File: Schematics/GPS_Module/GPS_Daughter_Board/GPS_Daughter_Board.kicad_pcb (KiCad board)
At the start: 2 copper layers, 50 x 65 mm, 22 parts, among them J2 470804001, U1 SAM-M10Q, U2 LM66100DCKR

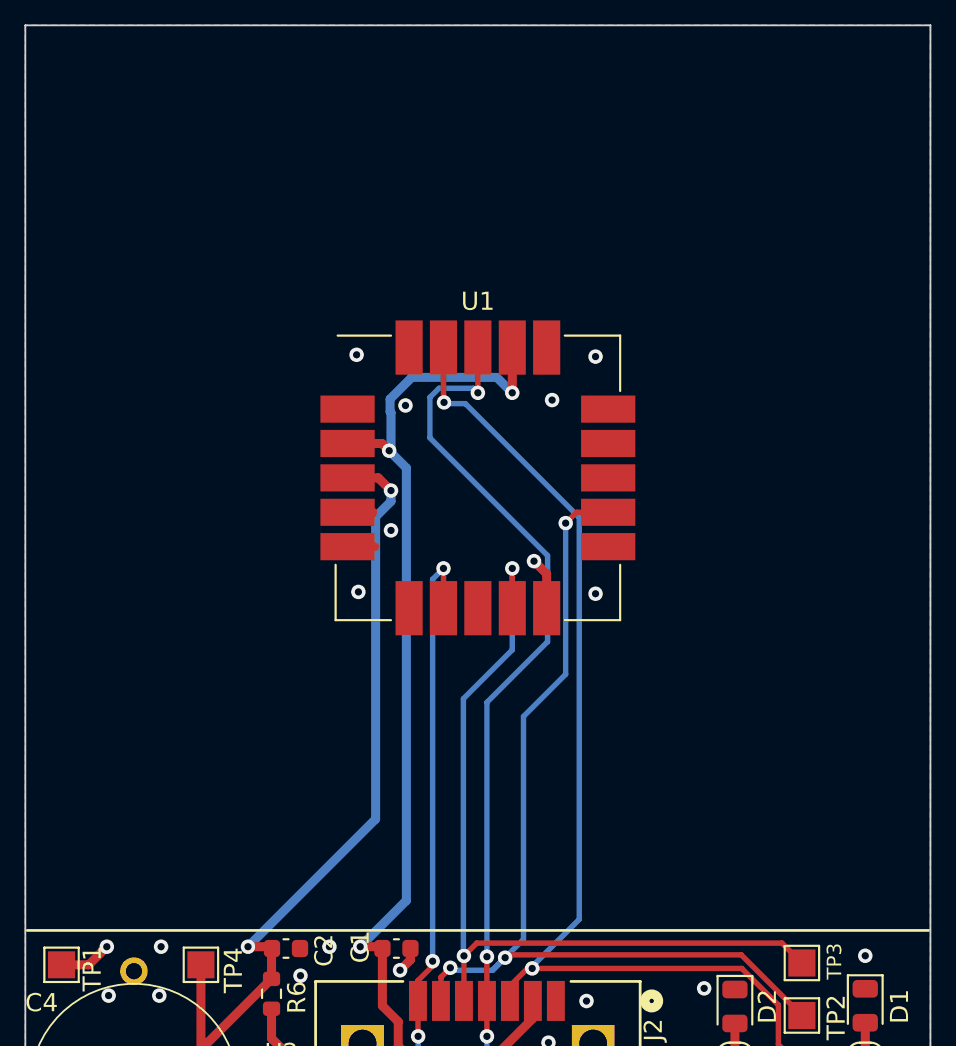
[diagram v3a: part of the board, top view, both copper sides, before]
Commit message: acutally finished GND stitching
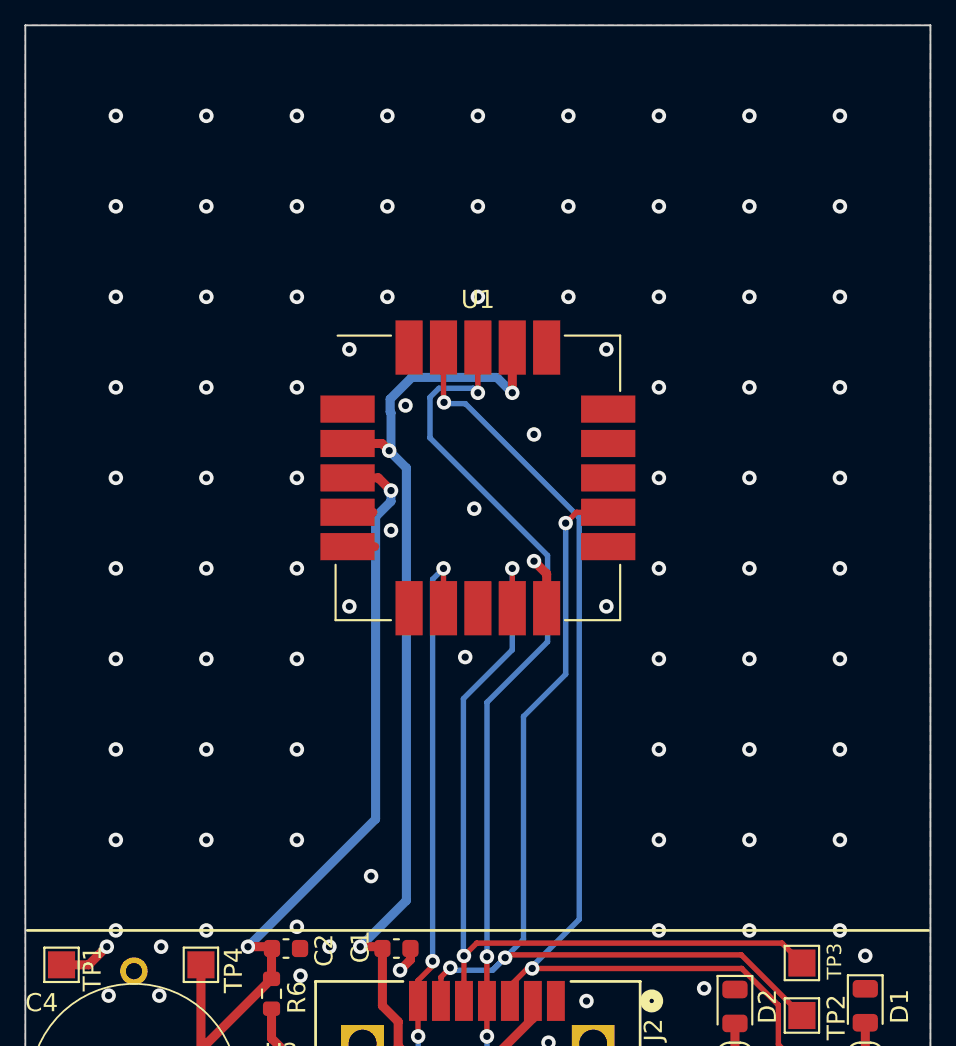
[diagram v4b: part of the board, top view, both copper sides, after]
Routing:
- net GPS_GND: vias 20 -> 92
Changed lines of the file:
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@@
     (property "ki_keywords" "gps module with antenna")
     (attr smd)
-    (fp_text reference "U1" (at 0 -9.75) (layer "F.SilkS")
+    (fp_text reference "U1" (at 0 -9.85) (layer "F.SilkS")
         (effects (font (size 1 1) (thickness 0.15)))
     )
@@
   (segment (start 142.0005 103) (end 140.5 103) (width 0.5) (layer "F.Cu") (net 1))
   (segment (start 141.9005 101.1) (end 140.5 101.1) (width 0.5) (layer "F.Cu") (net 1))
-  (via (at 154.2 105.6) (size 0.8) (drill 0.4) (layers "F.Cu" "B.Cu") (free) (net 1))
-  (via (at 141.1 105.5) (size 0.8) (drill 0.4) (layers "F.Cu" "B.Cu") (free) (net 1))
+  (via (at 132.7 104.2) (size 0.8) (drill 0.4) (layers "F.Cu" "B.Cu") (free) (net 1))
+  (via (at 152.7 79.2) (size 0.8) (drill 0.4) (layers "F.Cu" "B.Cu") (free) (net 1))
+  (via (at 127.7 99.2) (size 0.8) (drill 0.4) (layers "F.Cu" "B.Cu") (free) (net 1))
+  (via (at 137.7 104.2) (size 0.8) (drill 0.4) (layers "F.Cu" "B.Cu") (free) (net 1))
+  (via (at 154.8 106.3) (size 0.8) (drill 0.4) (layers "F.Cu" "B.Cu") (free) (net 1))
+  (via (at 127.7 124.2) (size 0.8) (drill 0.4) (layers "F.Cu" "B.Cu") (free) (net 1))
+  (via (at 137.7 114.2) (size 0.8) (drill 0.4) (layers "F.Cu" "B.Cu") (free) (net 1))
+  (via (at 140.6 106.3) (size 0.8) (drill 0.4) (layers "F.Cu" "B.Cu") (free) (net 1))
+  (via (at 127.7 94.2) (size 0.8) (drill 0.4) (layers "F.Cu" "B.Cu") (free) (net 1))
   (via (at 130.2 125.1) (size 0.8) (drill 0.4) (layers "F.Cu" "B.Cu") (free) (net 1))
+  (via (at 127.7 109.2) (size 0.8) (drill 0.4) (layers "F.Cu" "B.Cu") (free) (net 1))
+  (via (at 157.7 79.2) (size 0.8) (drill 0.4) (layers "F.Cu" "B.Cu") (free) (net 1))
+  (via (at 167.7 89.2) (size 0.8) (drill 0.4) (layers "F.Cu" "B.Cu") (free) (net 1))
+  (via (at 137.7 119.2) (size 0.8) (drill 0.4) (layers "F.Cu" "B.Cu") (free) (net 1))
+  (via (at 162.7 94.2) (size 0.8) (drill 0.4) (layers "F.Cu" "B.Cu") (free) (net 1))
+  (via (at 157.7 114.2) (size 0.8) (drill 0.4) (layers "F.Cu" "B.Cu") (free) (net 1))
+  (via (at 152.7 89.2) (size 0.8) (drill 0.4) (layers "F.Cu" "B.Cu") (free) (net 1))
+  (via (at 147.7 89.2) (size 0.8) (drill 0.4) (layers "F.Cu" "B.Cu") (free) (net 1))
+  (via (at 142.7 84.2) (size 0.8) (drill 0.4) (layers "F.Cu" "B.Cu") (free) (net 1))
+  (via (at 162.7 79.2) (size 0.8) (drill 0.4) (layers "F.Cu" "B.Cu") (free) (net 1))
+  (via (at 167.7 109.2) (size 0.8) (drill 0.4) (layers "F.Cu" "B.Cu") (free) (net 1))
+  (via (at 167.7 79.2) (size 0.8) (drill 0.4) (layers "F.Cu" "B.Cu") (free) (net 1))
+  (via (at 147.7 79.2) (size 0.8) (drill 0.4) (layers "F.Cu" "B.Cu") (free) (net 1))
+  (via (at 162.7 84.2) (size 0.8) (drill 0.4) (layers "F.Cu" "B.Cu") (free) (net 1))
+  (via (at 137.7 89.2) (size 0.8) (drill 0.4) (layers "F.Cu" "B.Cu") (free) (net 1))
+  (via (at 157.7 109.2) (size 0.8) (drill 0.4) (layers "F.Cu" "B.Cu") (free) (net 1))
   (via (at 143.7 95.2) (size 0.8) (drill 0.4) (layers "F.Cu" "B.Cu") (free) (net 1))
+  (via (at 132.7 109.2) (size 0.8) (drill 0.4) (layers "F.Cu" "B.Cu") (free) (net 1))
+  (via (at 137.7 94.2) (size 0.8) (drill 0.4) (layers "F.Cu" "B.Cu") (free) (net 1))
+  (via (at 127.7 84.2) (size 0.8) (drill 0.4) (layers "F.Cu" "B.Cu") (free) (net 1))
+  (via (at 167.7 124.2) (size 0.8) (drill 0.4) (layers "F.Cu" "B.Cu") (free) (net 1))
   (via (at 127.2 125.1) (size 0.8) (drill 0.4) (layers "F.Cu" "B.Cu") (free) (net 1))
+  (via (at 142.7 79.2) (size 0.8) (drill 0.4) (layers "F.Cu" "B.Cu") (free) (net 1))
+  (via (at 137.7 99.2) (size 0.8) (drill 0.4) (layers "F.Cu" "B.Cu") (free) (net 1))
+  (via (at 127.7 114.2) (size 0.8) (drill 0.4) (layers "F.Cu" "B.Cu") (free) (net 1))
   (via (at 153.7 128.1) (size 0.8) (drill 0.4) (layers "F.Cu" "B.Cu") (free) (net 1))
+  (via (at 132.7 114.2) (size 0.8) (drill 0.4) (layers "F.Cu" "B.Cu") (free) (net 1))
+  (via (at 132.7 124.2) (size 0.8) (drill 0.4) (layers "F.Cu" "B.Cu") (free) (net 1))
+  (via (at 157.7 119.2) (size 0.8) (drill 0.4) (layers "F.Cu" "B.Cu") (free) (net 1))
   (via (at 151.6 130.4) (size 0.8) (drill 0.4) (layers "F.Cu" "B.Cu") (free) (net 1))
+  (via (at 152.7 84.2) (size 0.8) (drill 0.4) (layers "F.Cu" "B.Cu") (free) (net 1))
+  (via (at 132.7 119.2) (size 0.8) (drill 0.4) (layers "F.Cu" "B.Cu") (free) (net 1))
   (via (at 130.1 127.8) (size 0.8) (drill 0.4) (layers "F.Cu" "B.Cu") (free) (net 1))
+  (via (at 157.7 104.2) (size 0.8) (drill 0.4) (layers "F.Cu" "B.Cu") (free) (net 1))
+  (via (at 132.7 99.2) (size 0.8) (drill 0.4) (layers "F.Cu" "B.Cu") (free) (net 1))
   (via (at 127.3 127.8) (size 0.8) (drill 0.4) (layers "F.Cu" "B.Cu") (free) (net 1))
-  (via (at 141 92.4) (size 0.8) (drill 0.4) (layers "F.Cu" "B.Cu") (free) (net 1))
+  (via (at 140.6 92.1) (size 0.8) (drill 0.4) (layers "F.Cu" "B.Cu") (free) (net 1))
+  (via (at 157.7 84.2) (size 0.8) (drill 0.4) (layers "F.Cu" "B.Cu") (free) (net 1))
   (via (at 139.5 125.1) (size 0.8) (drill 0.4) (layers "F.Cu" "B.Cu") (free) (net 1))
   (via (at 142.9005 102.1) (size 0.8) (drill 0.4) (layers "F.Cu" "B.Cu") (net 1))
+  (via (at 132.7 89.2) (size 0.8) (drill 0.4) (layers "F.Cu" "B.Cu") (free) (net 1))
+  (via (at 142.7 89.2) (size 0.8) (drill 0.4) (layers "F.Cu" "B.Cu") (free) (net 1))
+  (via (at 167.7 84.2) (size 0.8) (drill 0.4) (layers "F.Cu" "B.Cu") (free) (net 1))
+  (via (at 167.7 104.2) (size 0.8) (drill 0.4) (layers "F.Cu" "B.Cu") (free) (net 1))
+  (via (at 147.7 84.2) (size 0.8) (drill 0.4) (layers "F.Cu" "B.Cu") (free) (net 1))
+  (via (at 157.7 99.2) (size 0.8) (drill 0.4) (layers "F.Cu" "B.Cu") (free) (net 1))
+  (via (at 162.7 124.2) (size 0.8) (drill 0.4) (layers "F.Cu" "B.Cu") (free) (net 1))
+  (via (at 162.7 104.2) (size 0.8) (drill 0.4) (layers "F.Cu" "B.Cu") (free) (net 1))
+  (via (at 137.7 109.2) (size 0.8) (drill 0.4) (layers "F.Cu" "B.Cu") (free) (net 1))
   (via (at 136.8745 136.5) (size 0.8) (drill 0.4) (layers "F.Cu" "B.Cu") (net 1))
+  (via (at 157.7 124.2) (size 0.8) (drill 0.4) (layers "F.Cu" "B.Cu") (free) (net 1))
+  (via (at 137.7 84.2) (size 0.8) (drill 0.4) (layers "F.Cu" "B.Cu") (free) (net 1))
+  (via (at 127.7 79.2) (size 0.8) (drill 0.4) (layers "F.Cu" "B.Cu") (free) (net 1))
+  (via (at 141.8 121.2) (size 0.8) (drill 0.4) (layers "F.Cu" "B.Cu") (free) (net 1))
+  (via (at 132.7 84.2) (size 0.8) (drill 0.4) (layers "F.Cu" "B.Cu") (free) (net 1))
+  (via (at 167.7 99.2) (size 0.8) (drill 0.4) (layers "F.Cu" "B.Cu") (free) (net 1))
+  (via (at 162.7 89.2) (size 0.8) (drill 0.4) (layers "F.Cu" "B.Cu") (free) (net 1))
+  (via (at 162.7 99.2) (size 0.8) (drill 0.4) (layers "F.Cu" "B.Cu") (free) (net 1))
+  (via (at 167.7 119.2) (size 0.8) (drill 0.4) (layers "F.Cu" "B.Cu") (free) (net 1))
+  (via (at 162.7 114.2) (size 0.8) (drill 0.4) (layers "F.Cu" "B.Cu") (free) (net 1))
+  (via (at 127.7 119.2) (size 0.8) (drill 0.4) (layers "F.Cu" "B.Cu") (free) (net 1))
   (via (at 137.9 126.7) (size 0.8) (drill 0.4) (layers "F.Cu" "B.Cu") (free) (net 1))
+  (via (at 167.7 94.2) (size 0.8) (drill 0.4) (layers "F.Cu" "B.Cu") (free) (net 1))
   (via (at 150.800352 103.799645) (size 0.8) (drill 0.4) (layers "F.Cu" "B.Cu") (net 1))
+  (via (at 127.7 89.2) (size 0.8) (drill 0.4) (layers "F.Cu" "B.Cu") (free) (net 1))
+  (via (at 157.7 89.2) (size 0.8) (drill 0.4) (layers "F.Cu" "B.Cu") (free) (net 1))
+  (via (at 162.7 109.2) (size 0.8) (drill 0.4) (layers "F.Cu" "B.Cu") (free) (net 1))
+  (via (at 137.7 124) (size 0.8) (drill 0.4) (layers "F.Cu" "B.Cu") (free) (net 1))
+  (via (at 162.7 119.2) (size 0.8) (drill 0.4) (layers "F.Cu" "B.Cu") (free) (net 1))
+  (via (at 147 109.1) (size 0.8) (drill 0.4) (layers "F.Cu" "B.Cu") (free) (net 1))
+  (via (at 137.7 79.2) (size 0.8) (drill 0.4) (layers "F.Cu" "B.Cu") (free) (net 1))
+  (via (at 127.7 104.2) (size 0.8) (drill 0.4) (layers "F.Cu" "B.Cu") (free) (net 1))
   (via (at 169.1 125.6) (size 0.8) (drill 0.4) (layers "F.Cu" "B.Cu") (free) (net 1))
+  (via (at 157.7 94.2) (size 0.8) (drill 0.4) (layers "F.Cu" "B.Cu") (free) (net 1))
   (via (at 160.2 127.4) (size 0.8) (drill 0.4) (layers "F.Cu" "B.Cu") (free) (net 1))
-  (via (at 154.2 92.5) (size 0.8) (drill 0.4) (layers "F.Cu" "B.Cu") (free) (net 1))
+  (via (at 147.5 100.9) (size 0.8) (drill 0.4) (layers "F.Cu" "B.Cu") (free) (net 1))
+  (via (at 132.7 94.2) (size 0.8) (drill 0.4) (layers "F.Cu" "B.Cu") (free) (net 1))
+  (via (at 154.8 92.1) (size 0.8) (drill 0.4) (layers "F.Cu" "B.Cu") (free) (net 1))
   (via (at 143.4 126.4) (size 0.8) (drill 0.4) (layers "F.Cu" "B.Cu") (net 1))
-  (via (at 151.8 94.9) (size 0.8) (drill 0.4) (layers "F.Cu" "B.Cu") (free) (net 1))
+  (via (at 167.7 114.2) (size 0.8) (drill 0.4) (layers "F.Cu" "B.Cu") (free) (net 1))
+  (via (at 132.7 79.2) (size 0.8) (drill 0.4) (layers "F.Cu" "B.Cu") (free) (net 1))
+  (via (at 150.8 96.8) (size 0.8) (drill 0.4) (layers "F.Cu" "B.Cu") (free) (net 1))
   (segment (start 161.9 135.825) (end 149.025 135.825) (width 0.5) (layer "F.Cu") (net 2))
   (segment (start 136.025 137.7) (end 136.025 135.275) (width 0.5) (layer "F.Cu") (net 2))
